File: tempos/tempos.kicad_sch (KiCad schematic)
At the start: 8 parts, among them SW1 SW_Push, SW2 SW_Push, U1 WeMos_D1_mini

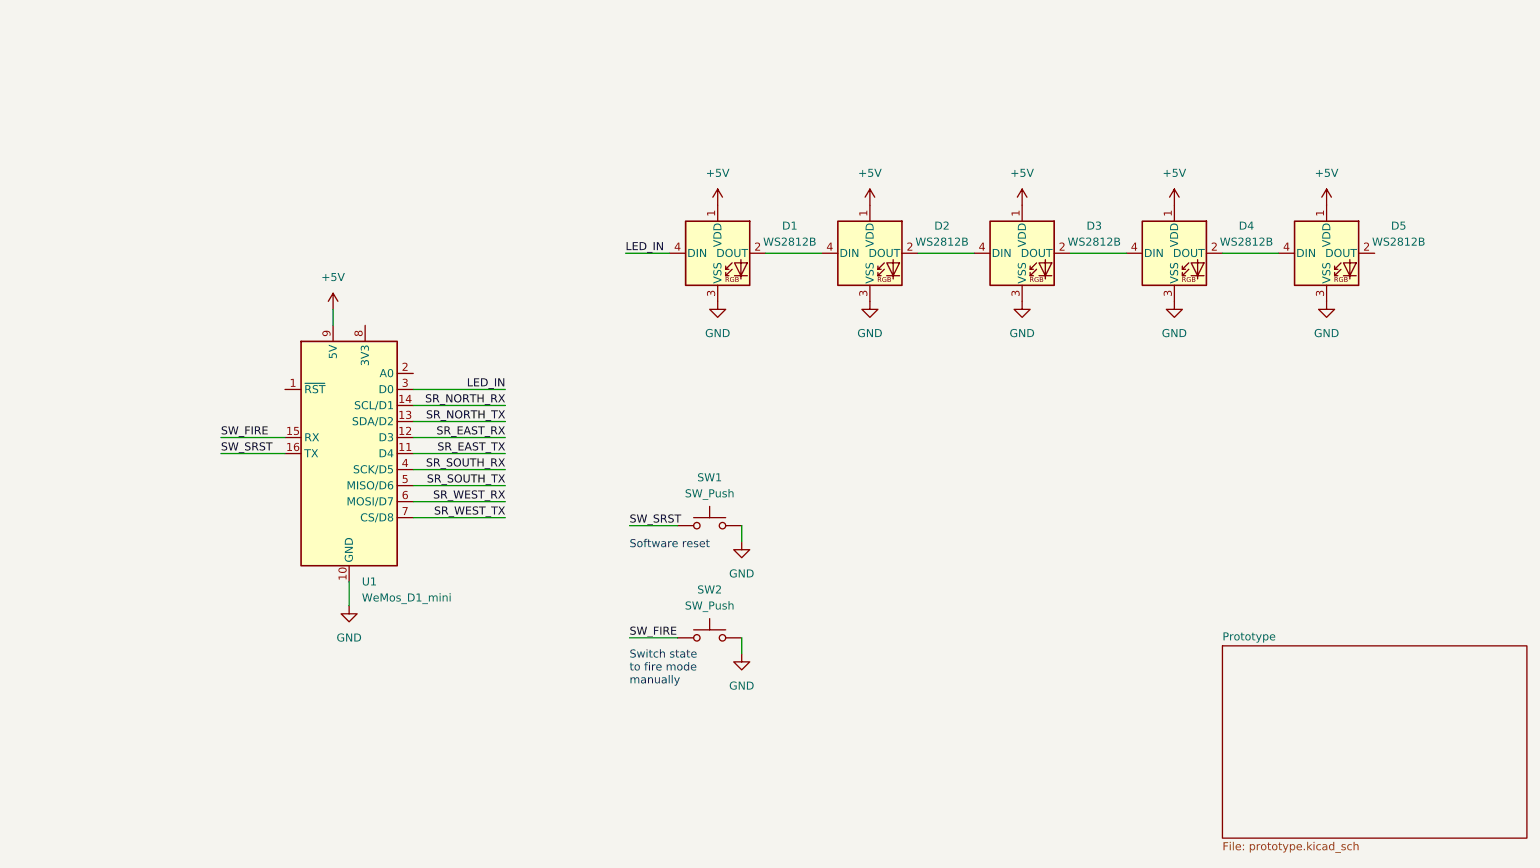
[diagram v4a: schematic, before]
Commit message: tempos: New node configuration with multiplexer
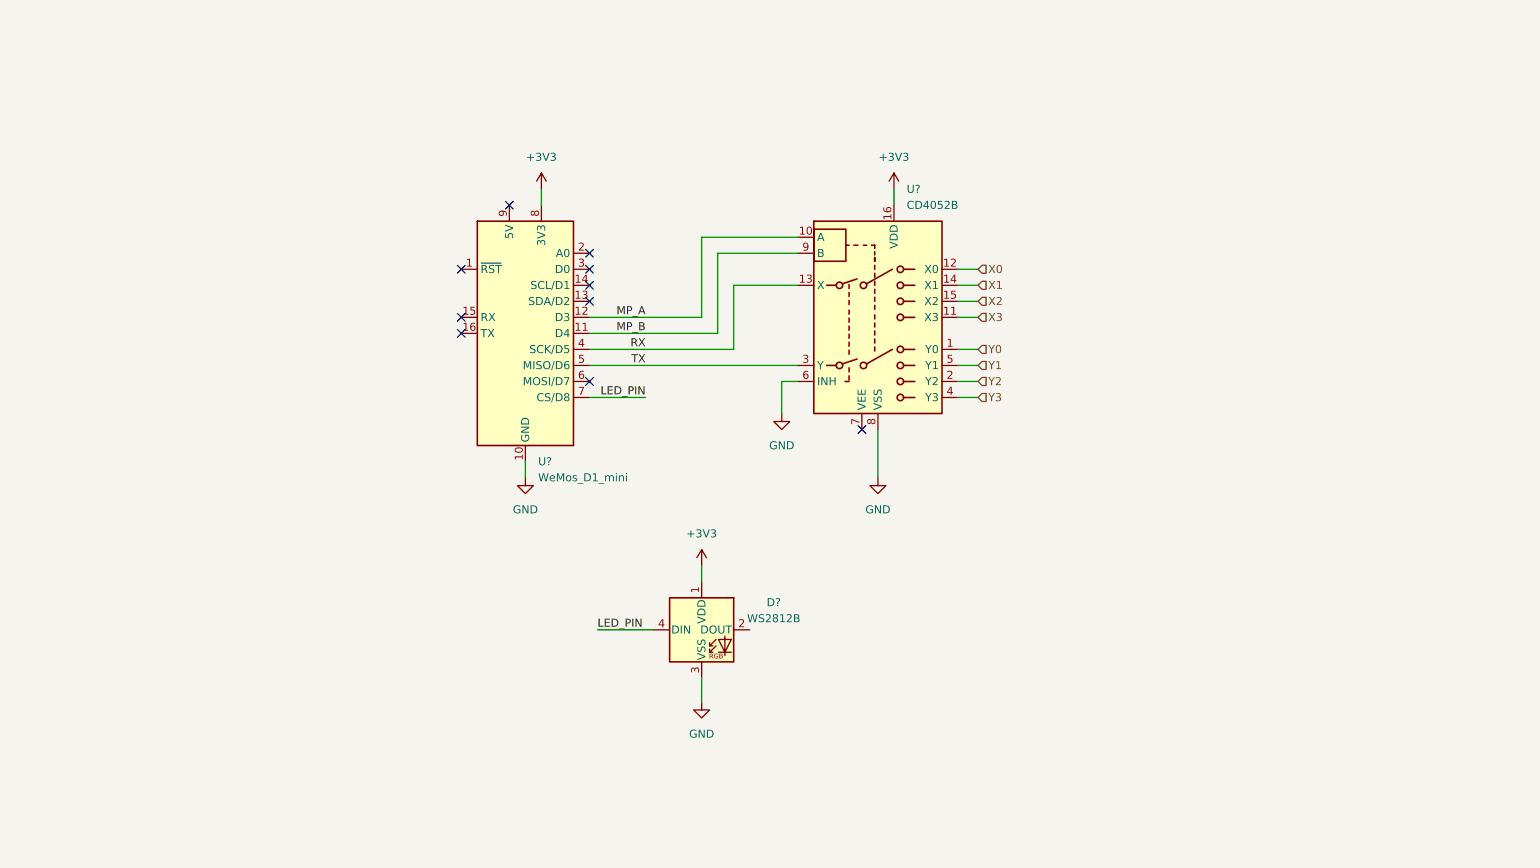
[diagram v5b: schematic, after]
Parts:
- removed D1, D2, D3, D4, D5: WS2812B, symbol tempos:WS2812B
- removed SW1, SW2: SW_Push, symbol Switch:SW_Push
- removed U1: WeMos_D1_mini, Module:WEMOS_D1_mini_light, symbol MCU_Module:WeMos_D1_mini
- added D?: WS2812B, symbol tempos:WS2812B
- added U?: CD4052B, symbol Analog_Switch:CD4052B
- added U?: WeMos_D1_mini, Module:WEMOS_D1_mini_light, symbol MCU_Module:WeMos_D1_mini
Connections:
- net GND: now also D?.3 (VSS), U?.10 (GND), U?.6 (INH), U?.8 (VSS)
- new net +3V3: D?.1 (VDD), U?.16 (VDD), U?.8 (3V3)
- new net LED_PIN: D?.4 (DIN), U?.7 (CS/D8)
- new net MP_A: U?.10 (A), U?.12 (D3)
- new net MP_B: U?.11 (D4), U?.9 (B)
- new net RX: U?.13 (X), U?.4 (SCK/D5)
- new net TX: U?.3 (Y), U?.5 (MISO/D6)
- new net X0: U?.12 (X0)
- new net X1: U?.14 (X1)
- new net X2: U?.15 (X2)
- new net X3: U?.11 (X3)
- new net Y0: U?.1 (Y0)
- new net Y1: U?.5 (Y1)
- new net Y2: U?.2 (Y2)
- new net Y3: U?.4 (Y3)
- no-connect marks 0 -> 10
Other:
- removed sheet Prototype
- note removed: "Software reset"
- note removed: "Switch state to fire mode manually"
- company: Malmö Universitet -> Malmö Universitet, Fakulteten för teknik och samhälle
- title: tempos -> tempos single node

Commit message: tempos: New hardware configuration
Multiplexer with MAX3485 and shift register.

This tries to fix the pin assignment problem and use only two wire for
communication between devices instead of having three, two being signal
cable and one being ground.
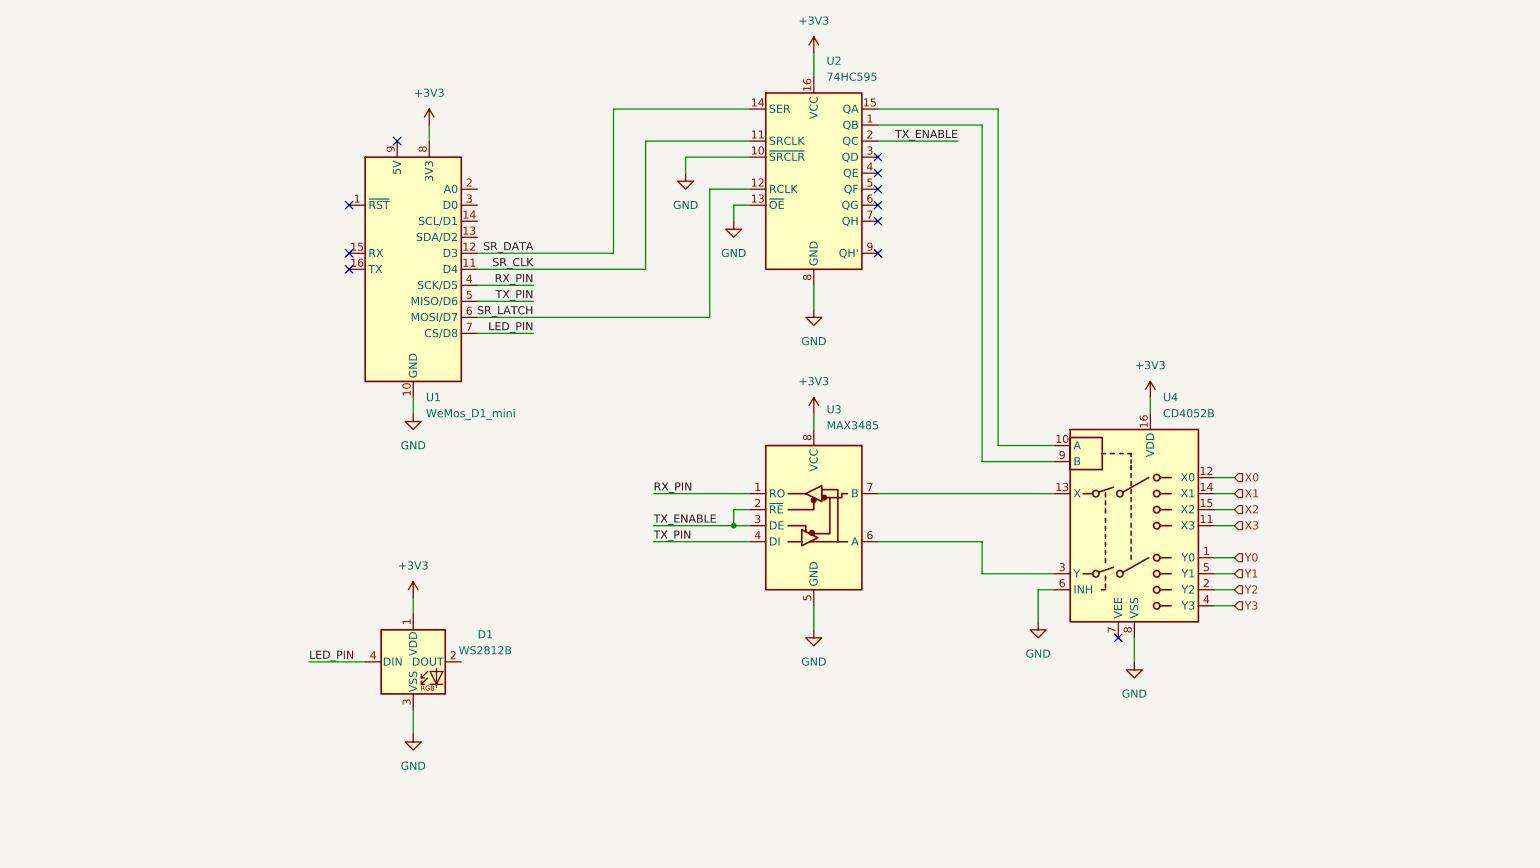
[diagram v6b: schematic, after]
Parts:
- added U2: 74HC595, symbol 74xx:74HC595
- added U3: MAX3485, symbol Interface_UART:MAX3485
- gave numbers to parts that had none: 3
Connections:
- net +3V3: now also U2.16 (VCC), U3.8 (VCC)
- net GND: now also U2.10 (~{SRCLR}), U2.13 (~{OE}), U2.8 (GND), U3.5 (GND)
- net SR_LATCH: now reaches U1.6 (MOSI/D7)
- net SR_LATCH: now also U2.12 (RCLK)
- net MP_A: no longer names the net of U4.10 (A)
- net MP_A: now also U2.15 (QA); no longer U1.12 (D3)
- net MP_B: no longer names the net of U4.9 (B)
- net MP_B: now also U2.1 (QB); no longer U1.11 (D4)
- net RX: no longer names the net of U4.13 (X)
- net RX: now also U3.7 (B); no longer U1.4 (SCK/D5)
- net TX: no longer names the net of U4.3 (Y)
- net TX: now also U3.6 (A); no longer U1.5 (MISO/D6)
- new net RX_PIN: U1.4 (SCK/D5), U3.1 (RO)
- new net SR_CLK: U1.11 (D4), U2.11 (SRCLK)
- new net SR_DATA: U1.12 (D3), U2.14 (SER)
- new net TX_ENABLE: U2.2 (QC), U3.2 (~{RE}), U3.3 (DE)
- new net TX_PIN: U1.5 (MISO/D6), U3.4 (DI)
- no-connect marks 10 -> 11
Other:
- moved on the sheet: D1, U1, U4

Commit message: tempos: Missing ground pin VEE for multiplex
Without pulling this to a known voltage value we're getting a really
weird data when switching between different channels.
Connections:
- net +3V3: now also U2.10 (~{SRCLR})
- net GND: now also U4.7 (VEE); no longer U2.10 (~{SRCLR})
- no-connect marks 11 -> 10
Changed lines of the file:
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@@
     (company "Malmö Universitet, Fakulteten för teknik och samhälle")
     (comment 3 "Copyright: Malmö Universitet")
-    (comment 4 "Author: Pratchaya Khansomboon, Linnea Mörk")
+    (comment 4 "Author: Pratchaya Khansomboon")
   )
   (junction (at 147.32 107.95) (diameter 0) (color 0 0 0 0)
   )
-  (no_connect (at 208.28 125.73))
+  (junction (at 210.82 127.635) (diameter 0) (color 0 0 0 0)
+  )
   (no_connect (at 170.18 49.53))
   (no_connect (at 86.36 64.77))
@@
   (no_connect (at 170.18 64.77))
   (no_connect (at 93.98 46.99))
+  (wire (pts (xy 210.82 127.635) (xy 210.82 129.54))
+    (stroke (width 0) (type default) (color 0 0 0 0))
+  )
+  (wire (pts (xy 106.68 74.93) (xy 133.35 74.93))
+    (stroke (width 0) (type default) (color 0 0 0 0))
+  )
   (wire (pts (xy 80.01 129.54) (xy 88.9 129.54))
     (stroke (width 0) (type default) (color 0 0 0 0))
@@
     (stroke (width 0) (type default) (color 0 0 0 0))
   )
+  (wire (pts (xy 143.51 33.02) (xy 143.51 49.53))
+    (stroke (width 0) (type default) (color 0 0 0 0))
+  )
   (wire (pts (xy 96.52 119.38) (xy 96.52 121.92))
     (stroke (width 0) (type default) (color 0 0 0 0))
   )
-  (wire (pts (xy 149.86 41.91) (xy 128.27 41.91))
-    (stroke (width 0) (type default) (color 0 0 0 0))
-  )
-  (wire (pts (xy 133.35 67.31) (xy 106.68 67.31))
-    (stroke (width 0) (type default) (color 0 0 0 0))
-  )
   (wire (pts (xy 147.32 107.95) (xy 149.86 107.95))
     (stroke (width 0) (type default) (color 0 0 0 0))
   )
-  (wire (pts (xy 143.51 54.61) (xy 143.51 74.93))
+  (wire (pts (xy 133.35 54.61) (xy 133.35 74.93))
+    (stroke (width 0) (type default) (color 0 0 0 0))
+  )
+  (wire (pts (xy 129.54 46.99) (xy 129.54 67.31))
     (stroke (width 0) (type default) (color 0 0 0 0))
   )
@@
     (stroke (width 0) (type default) (color 0 0 0 0))
   )
+  (wire (pts (xy 125.73 64.77) (xy 106.68 64.77))
+    (stroke (width 0) (type default) (color 0 0 0 0))
+  )
   (wire (pts (xy 106.68 72.39) (xy 115.57 72.39))
     (stroke (width 0) (type default) (color 0 0 0 0))
@@
     (stroke (width 0) (type default) (color 0 0 0 0))
   )
-  (wire (pts (xy 106.68 74.93) (xy 143.51 74.93))
-    (stroke (width 0) (type default) (color 0 0 0 0))
-  )
   (wire (pts (xy 223.52 100.33) (xy 226.695 100.33))
     (stroke (width 0) (type default) (color 0 0 0 0))
   )
-  (wire (pts (xy 149.86 49.53) (xy 139.7 49.53))
-    (stroke (width 0) (type default) (color 0 0 0 0))
-  )
-  (wire (pts (xy 149.86 54.61) (xy 143.51 54.61))
-    (stroke (width 0) (type default) (color 0 0 0 0))
-  )
   (wire (pts (xy 149.86 57.15) (xy 147.32 57.15))
     (stroke (width 0) (type default) (color 0 0 0 0))
@@
     (stroke (width 0) (type default) (color 0 0 0 0))
   )
-  (wire (pts (xy 128.27 41.91) (xy 128.27 64.77))
-    (stroke (width 0) (type default) (color 0 0 0 0))
-  )
   (wire (pts (xy 134.62 107.95) (xy 147.32 107.95))
     (stroke (width 0) (type default) (color 0 0 0 0))
@@
     (stroke (width 0) (type default) (color 0 0 0 0))
   )
+  (wire (pts (xy 129.54 67.31) (xy 106.68 67.31))
+    (stroke (width 0) (type default) (color 0 0 0 0))
+  )
+  (wire (pts (xy 149.86 46.99) (xy 129.54 46.99))
+    (stroke (width 0) (type default) (color 0 0 0 0))
+  )
   (wire (pts (xy 189.23 41.91) (xy 189.23 95.25))
     (stroke (width 0) (type default) (color 0 0 0 0))
@@
     (stroke (width 0) (type default) (color 0 0 0 0))
   )
+  (wire (pts (xy 125.73 41.91) (xy 149.86 41.91))
+    (stroke (width 0) (type default) (color 0 0 0 0))
+  )
   (wire (pts (xy 223.52 105.41) (xy 226.695 105.41))
     (stroke (width 0) (type default) (color 0 0 0 0))
@@
     (stroke (width 0) (type default) (color 0 0 0 0))
   )
-  (wire (pts (xy 139.7 49.53) (xy 139.7 52.07))
+  (wire (pts (xy 125.73 41.91) (xy 125.73 64.77))
     (stroke (width 0) (type default) (color 0 0 0 0))
   )
@@
     (stroke (width 0) (type default) (color 0 0 0 0))
   )
-  (wire (pts (xy 133.35 46.99) (xy 133.35 67.31))
+  (wire (pts (xy 208.28 125.73) (xy 208.28 127.635))
     (stroke (width 0) (type default) (color 0 0 0 0))
   )
@@
     (stroke (width 0) (type default) (color 0 0 0 0))
   )
+  (wire (pts (xy 149.86 54.61) (xy 133.35 54.61))
+    (stroke (width 0) (type default) (color 0 0 0 0))
+  )
   (wire (pts (xy 223.52 113.03) (xy 226.695 113.03))
     (stroke (width 0) (type default) (color 0 0 0 0))
   )
-  (wire (pts (xy 149.86 46.99) (xy 133.35 46.99))
-    (stroke (width 0) (type default) (color 0 0 0 0))
-  )
   (wire (pts (xy 186.69 97.79) (xy 198.12 97.79))
     (stroke (width 0) (type default) (color 0 0 0 0))
@@
     (stroke (width 0) (type default) (color 0 0 0 0))
   )
-  (wire (pts (xy 210.82 125.73) (xy 210.82 129.54))
+  (wire (pts (xy 210.82 125.73) (xy 210.82 127.635))
     (stroke (width 0) (type default) (color 0 0 0 0))
   )
@@
     (stroke (width 0) (type default) (color 0 0 0 0))
   )
+  (wire (pts (xy 143.51 49.53) (xy 149.86 49.53))
+    (stroke (width 0) (type default) (color 0 0 0 0))
+  )
   (wire (pts (xy 170.18 41.91) (xy 189.23 41.91))
     (stroke (width 0) (type default) (color 0 0 0 0))
@@
     (stroke (width 0) (type default) (color 0 0 0 0))
   )
-  (wire (pts (xy 128.27 64.77) (xy 106.68 64.77))
+  (wire (pts (xy 208.28 127.635) (xy 210.82 127.635))
     (stroke (width 0) (type default) (color 0 0 0 0))
   )
@@
     (pin "1")
   )
-  (symbol (lib_id "power:GND") (at 139.7 52.07 0) (unit 1)
-    (in_bom yes) (on_board yes) (fields_autoplaced)
-    (property "Reference" "#PWR?" (id 0) (at 139.7 58.42 0)
-      (effects (font (size 1.27 1.27)) hide)
-    )
-    (property "Value" "GND" (id 1) (at 139.7 57.15 0))
-    (property "Footprint" "" (id 2) (at 139.7 52.07 0)
-      (effects (font (size 1.27 1.27)) hide)
-    )
-    (property "Datasheet" "" (id 3) (at 139.7 52.07 0)
-      (effects (font (size 1.27 1.27)) hide)
-    )
-    (pin "1")
-  )
   (symbol (lib_id "power:GND") (at 96.52 90.17 0) (unit 1)
     (in_bom yes) (on_board yes) (fields_autoplaced)
@@
     (pin "9")
   )
+  (symbol (lib_id "power:+3V3") (at 143.51 33.02 0) (unit 1)
+    (in_bom yes) (on_board yes) (fields_autoplaced)
+    (property "Reference" "#PWR?" (id 0) (at 143.51 36.83 0)
+      (effects (font (size 1.27 1.27)) hide)
+    )
+    (property "Value" "+3V3" (id 1) (at 143.51 27.94 0))
+    (property "Footprint" "" (id 2) (at 143.51 33.02 0)
+      (effects (font (size 1.27 1.27)) hide)
+    )
+    (property "Datasheet" "" (id 3) (at 143.51 33.02 0)
+      (effects (font (size 1.27 1.27)) hide)
+    )
+    (pin "1")
+  )
   (symbol (lib_id "power:GND") (at 160.02 73.66 0) (unit 1)
     (in_bom yes) (on_board yes) (fields_autoplaced)
@@
       (reference "#PWR?") (unit 1) (value "GND") (footprint "")
     )
-    (path "/959459a7-0e31-459f-a53f-cbd25b362e62"
-      (reference "#PWR?") (unit 1) (value "GND") (footprint "")
+    (path "/c3866304-54f7-4450-a334-3511022e9040"
+      (reference "#PWR?") (unit 1) (value "+3V3") (footprint "")
     )
     (path "/54611b69-1581-4074-a34f-767d9ae5be50"

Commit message: tempos: Added fire, reset switches.
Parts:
- added SW1, SW2: SW_Push, symbol Switch:SW_Push
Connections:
- net GND: now also SW1.2, SW2.2
- net SW_Fire: now reaches U1.13 (SDA/D2)
- net SW_Fire: now also SW2.1
- net SW_Reset: now reaches U1.14 (SCL/D1)
- net SW_Reset: now also SW1.1
